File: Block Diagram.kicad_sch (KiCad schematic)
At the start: 0 parts

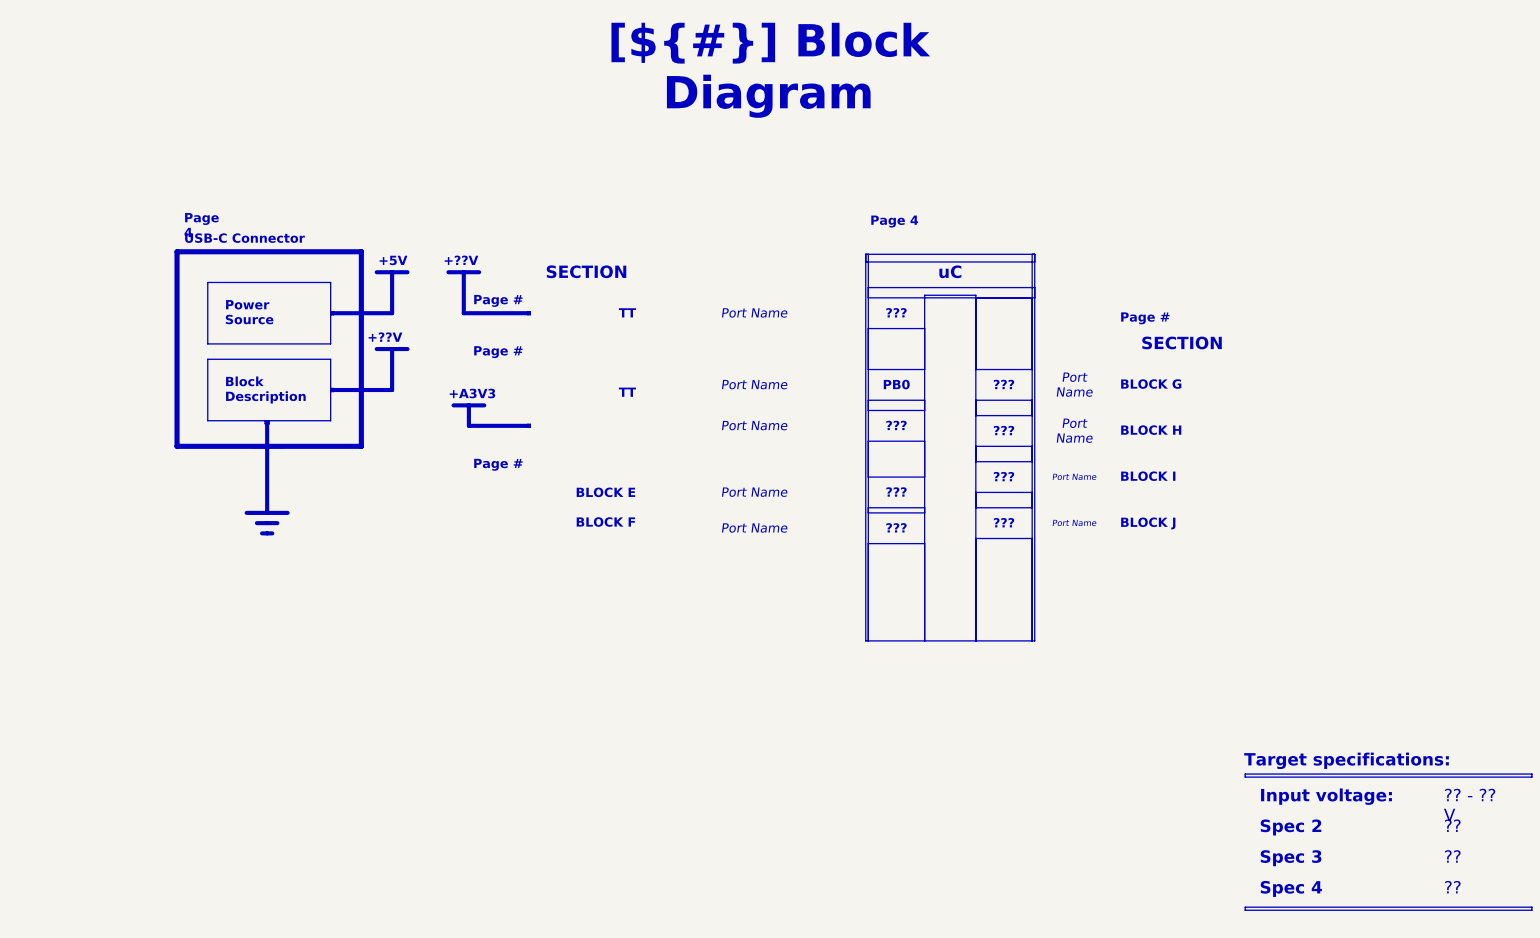
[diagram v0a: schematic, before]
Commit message: documentation update / block diagram
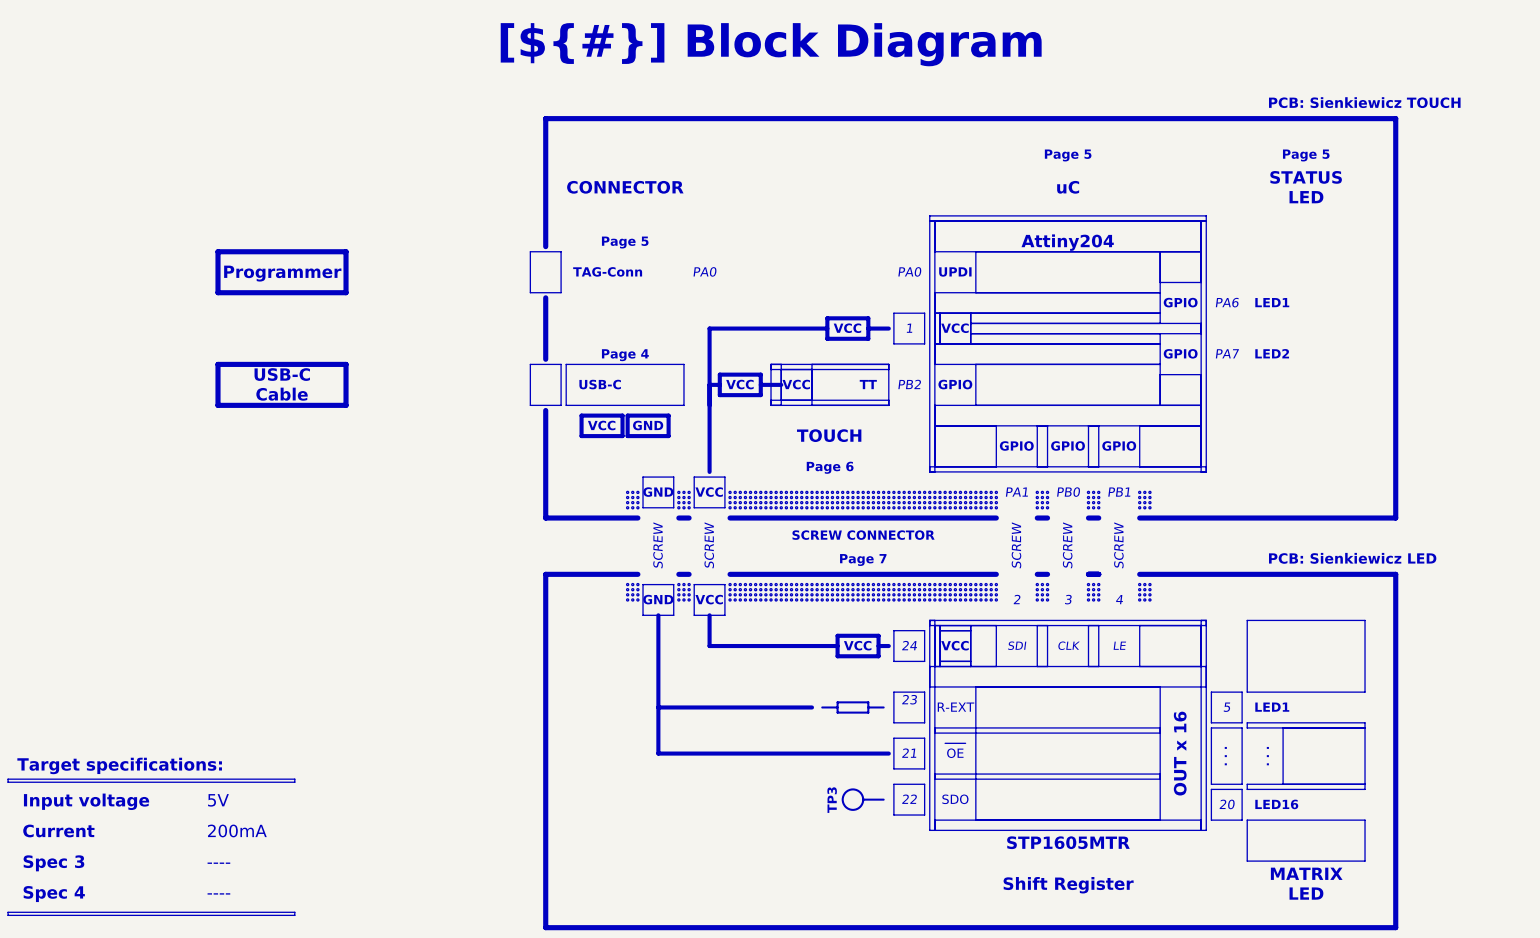
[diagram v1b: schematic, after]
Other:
- note added: "PCB: Sienkiewicz LED"
- note added: "PCB: Sienkiewicz TOUCH"
- note removed: "+5V"
- note removed: "+??V"
- note removed: "+A3V3"
